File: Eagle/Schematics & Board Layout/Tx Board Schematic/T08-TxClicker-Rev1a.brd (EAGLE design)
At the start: 83.8 x 42.2 mm, 98 parts, among them U1 CC430F513X---RGZ48, X1-DNI SMA-SMD, Y1 26MHz

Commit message: O.O
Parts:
- added X1-DNI1: SMA-SMD, con-coax:SMA-SMD
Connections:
- new net TEST50: X1-DNI1.1
- net GND: now also X1-DNI1.2@1, X1-DNI1.2@2, X1-DNI1.2@3, X1-DNI1.2@4, X1-DNI1.2@5, X1-DNI1.2@6
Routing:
- net TEST50: track 0.00 -> 5.08 mm
- net GND: track 9.81 -> 9.82 mm, vias 23 -> 152
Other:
- board text added: "Portland State University Team: T08 Nov2014 RevA"
- board text removed: "BOTTOM"
- board text removed: "Portland State University Team: T08 Nov2014"
- board text removed: "TOP"

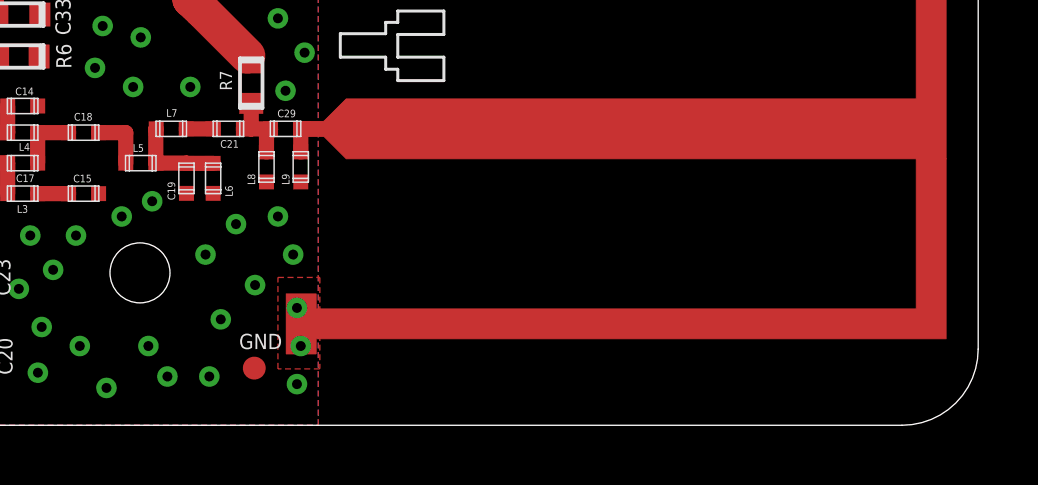
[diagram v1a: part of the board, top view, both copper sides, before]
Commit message: Updated silkscreen, added board preview
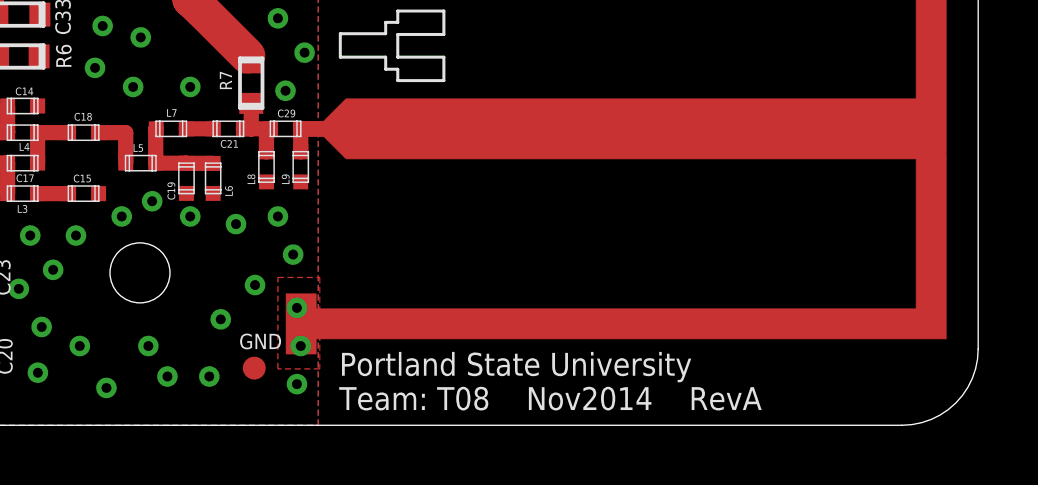
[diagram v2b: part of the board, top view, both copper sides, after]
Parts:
- renumbered X1-DNI1 to XCAL-DNI
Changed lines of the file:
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@@
 <?xml version="1.0" encoding="utf-8"?>
 <!DOCTYPE eagle SYSTEM "eagle.dtd">
-<eagle version="7.1.0">
+<eagle version="6.4">
 <drawing>
 <settings>
@@
 <layer number="20" name="Dimension" color="15" fill="1" visible="yes" active="yes"/>
 <layer number="21" name="tPlace" color="7" fill="1" visible="yes" active="yes"/>
-<layer number="22" name="bPlace" color="7" fill="1" visible="no" active="yes"/>
-<layer number="23" name="tOrigins" color="15" fill="1" visible="no" active="yes"/>
-<layer number="24" name="bOrigins" color="15" fill="1" visible="no" active="yes"/>
+<layer number="22" name="bPlace" color="7" fill="1" visible="yes" active="yes"/>
+<layer number="23" name="tOrigins" color="15" fill="1" visible="yes" active="yes"/>
+<layer number="24" name="bOrigins" color="15" fill="1" visible="yes" active="yes"/>
 <layer number="25" name="tNames" color="7" fill="1" visible="yes" active="yes"/>
 <layer number="26" name="bNames" color="7" fill="1" visible="yes" active="yes"/>
@@
 <wire x1="8.636" y1="0" x2="81.28" y2="0" width="0" layer="20"/>
 <wire x1="83.82" y1="2.54" x2="83.82" y2="39.624" width="0" layer="20"/>
-<text x="46.0121" y="31.623" size="1.524" layer="22" font="vector" rot="SMR0">Portland State University
-Team: T08    Nov2014    RevA
-</text>
+<text x="62.5221" y="0.508" size="0.762" layer="21" font="vector" rot="SR0">Portland State University
+Team: T08    Nov2014    RevA</text>
 <text x="44.323" y="22.352" size="5.08" layer="21" font="vector" rot="SR270">A</text>
 <text x="30.861" y="22.352" size="5.08" layer="21" font="vector" rot="SR270">B</text>
@@
 <pass name="Default">
 <param name="RoutingGrid" value="50mil"/>
-<param name="AutoGrid" value="1"/>
-<param name="Efforts" value="0"/>
-<param name="TopRouterVariant" value="1"/>
 <param name="tpViaShape" value="round"/>
 <param name="PrefDir.1" value="|"/>
@@
 <attribute name="NAME" x="25.4" y="3.9624" size="0.508" layer="25" font="vector"/>
 </element>
-<element name="X1-DNI1" library="con-coax" package="SMA-SMD" value="SMA-SMD" x="7.62" y="14.224" rot="MR0">
+<element name="XCAL-DNI" library="con-coax" package="SMA-SMD" value="SMA-SMD" x="7.62" y="14.224" smashed="yes" rot="MR0">
 <attribute name="OC_NEWARK" value="unknown" x="7.62" y="14.224" size="1.778" layer="28" rot="MR0" display="off"/>
 <attribute name="MPN" value="" x="7.62" y="14.224" size="1.778" layer="28" rot="MR0" display="off"/>
 <attribute name="MF" value="" x="7.62" y="14.224" size="1.778" layer="28" rot="MR0" display="off"/>
 <attribute name="OC_FARNELL" value="unknown" x="7.62" y="14.224" size="1.778" layer="28" rot="MR0" display="off"/>
+<attribute name="NAME" x="12.7" y="18.034" size="1.27" layer="26" rot="MR270"/>
+<attribute name="VALUE" x="10.795" y="8.509" size="1.27" layer="28" rot="MR0"/>
 </element>
 </elements>
@@
 <contactref element="C9" pad="2"/>
 <contactref element="C12" pad="2"/>
-<polygon width="0.254" layer="16">
+<polygon width="0.254" layer="16" isolate="0.254">
 <vertex x="0" y="0"/>
 <vertex x="61.8236" y="0"/>
@@
 <wire x1="40.64" y1="24.478" x2="40.632" y2="24.47" width="0.254" layer="1"/>
 <via x="48.2854" y="22.5806" extent="1-16" drill="0.3302"/>
-<contactref element="X1-DNI1" pad="2@1"/>
-<contactref element="X1-DNI1" pad="2@6"/>
-<contactref element="X1-DNI1" pad="2@5"/>
-<contactref element="X1-DNI1" pad="2@4"/>
-<contactref element="X1-DNI1" pad="2@2"/>
-<contactref element="X1-DNI1" pad="2@3"/>
+<contactref element="XCAL-DNI" pad="2@1"/>
+<contactref element="XCAL-DNI" pad="2@6"/>
+<contactref element="XCAL-DNI" pad="2@5"/>
+<contactref element="XCAL-DNI" pad="2@4"/>
+<contactref element="XCAL-DNI" pad="2@2"/>
+<contactref element="XCAL-DNI" pad="2@3"/>
 <wire x1="40.64" y1="22.86" x2="40.632" y2="22.86" width="0.254" layer="1"/>
 <via x="60.3504" y="40.6146" extent="1-16" drill="0.3302"/>
@@
 <via x="61.1124" y="1.3716" extent="1-16" drill="0.3302"/>
 <via x="58.1914" y="1.6256" extent="1-16" drill="0.3302"/>
-<via x="58.0644" y="5.6896" extent="1-16" drill="0.3302"/>
+<via x="57.5564" y="6.9596" extent="1-16" drill="0.3302"/>
 <via x="61.1124" y="3.9116" extent="1-16" drill="0.3302"/>
 <via x="61.2394" y="2.6416" extent="1-16" drill="0.3302"/>
@@
 </signal>
 <signal name="TEST50">
-<contactref element="X1-DNI1" pad="1"/>
+<contactref element="XCAL-DNI" pad="1"/>
 <wire x1="7.62" y1="14.224" x2="7.62" y2="9.144" width="1.1938" layer="16"/>
 </signal>
